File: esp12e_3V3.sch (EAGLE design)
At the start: 26 parts, among them IC1 117\33

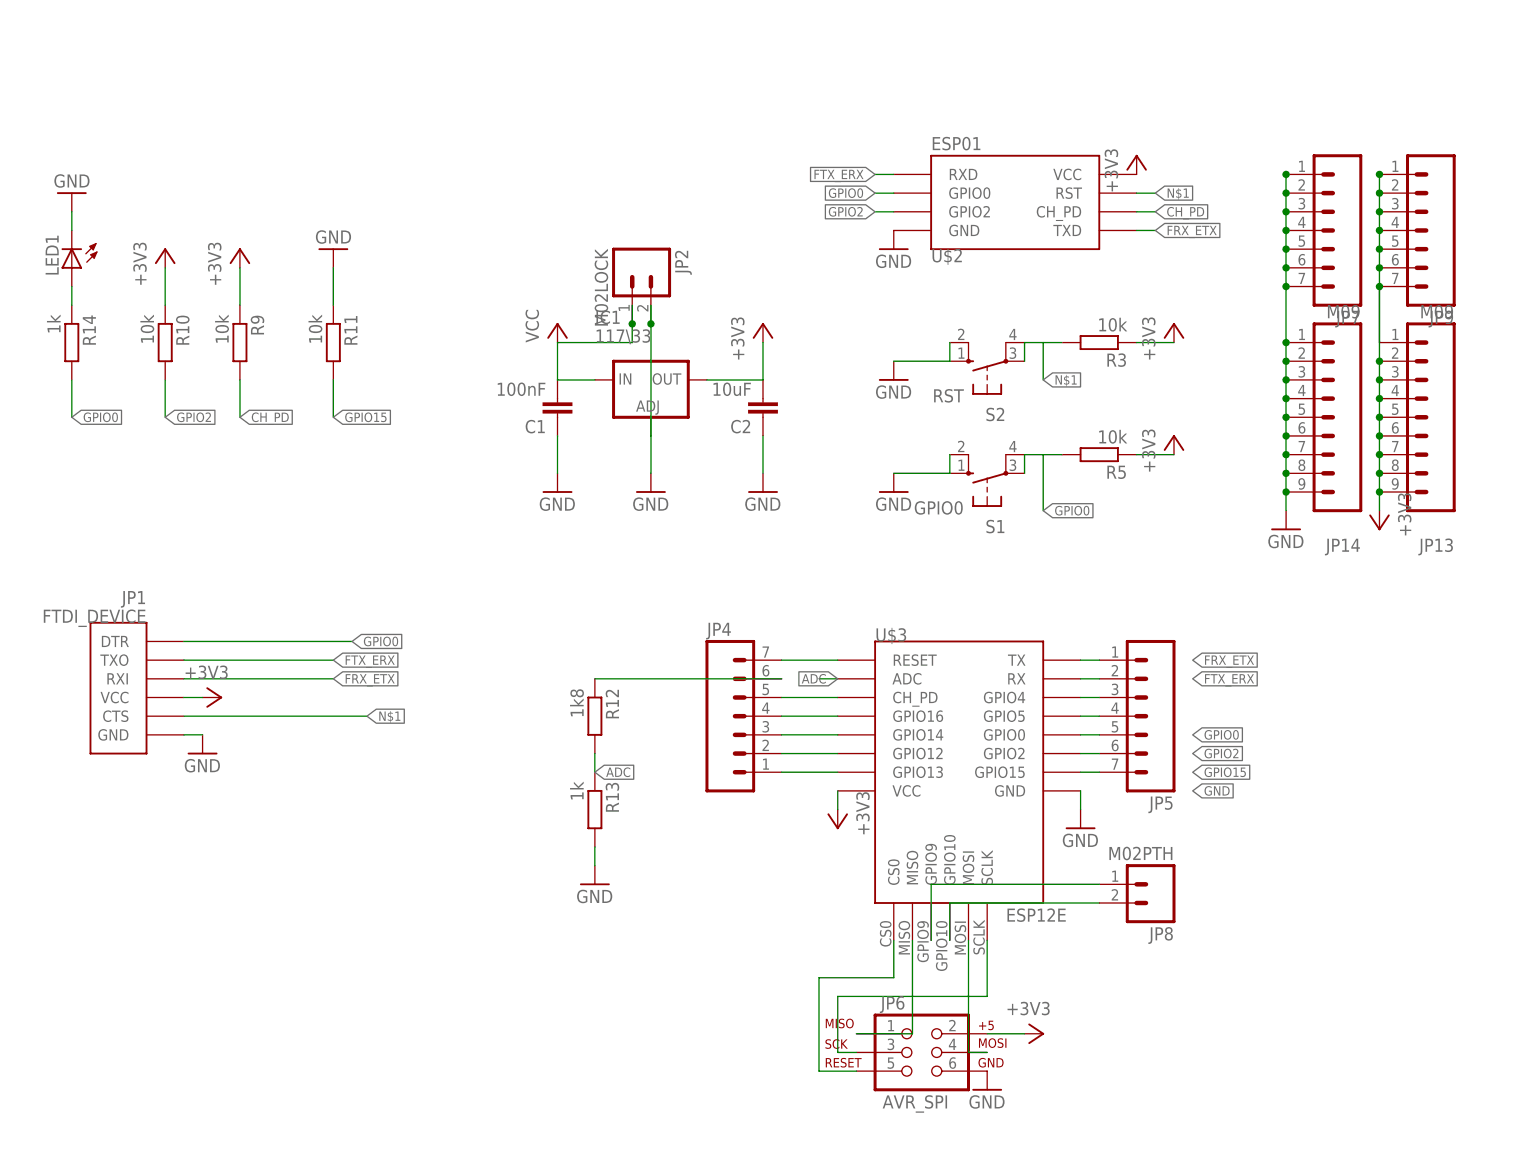
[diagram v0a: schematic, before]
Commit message: esp12e revision
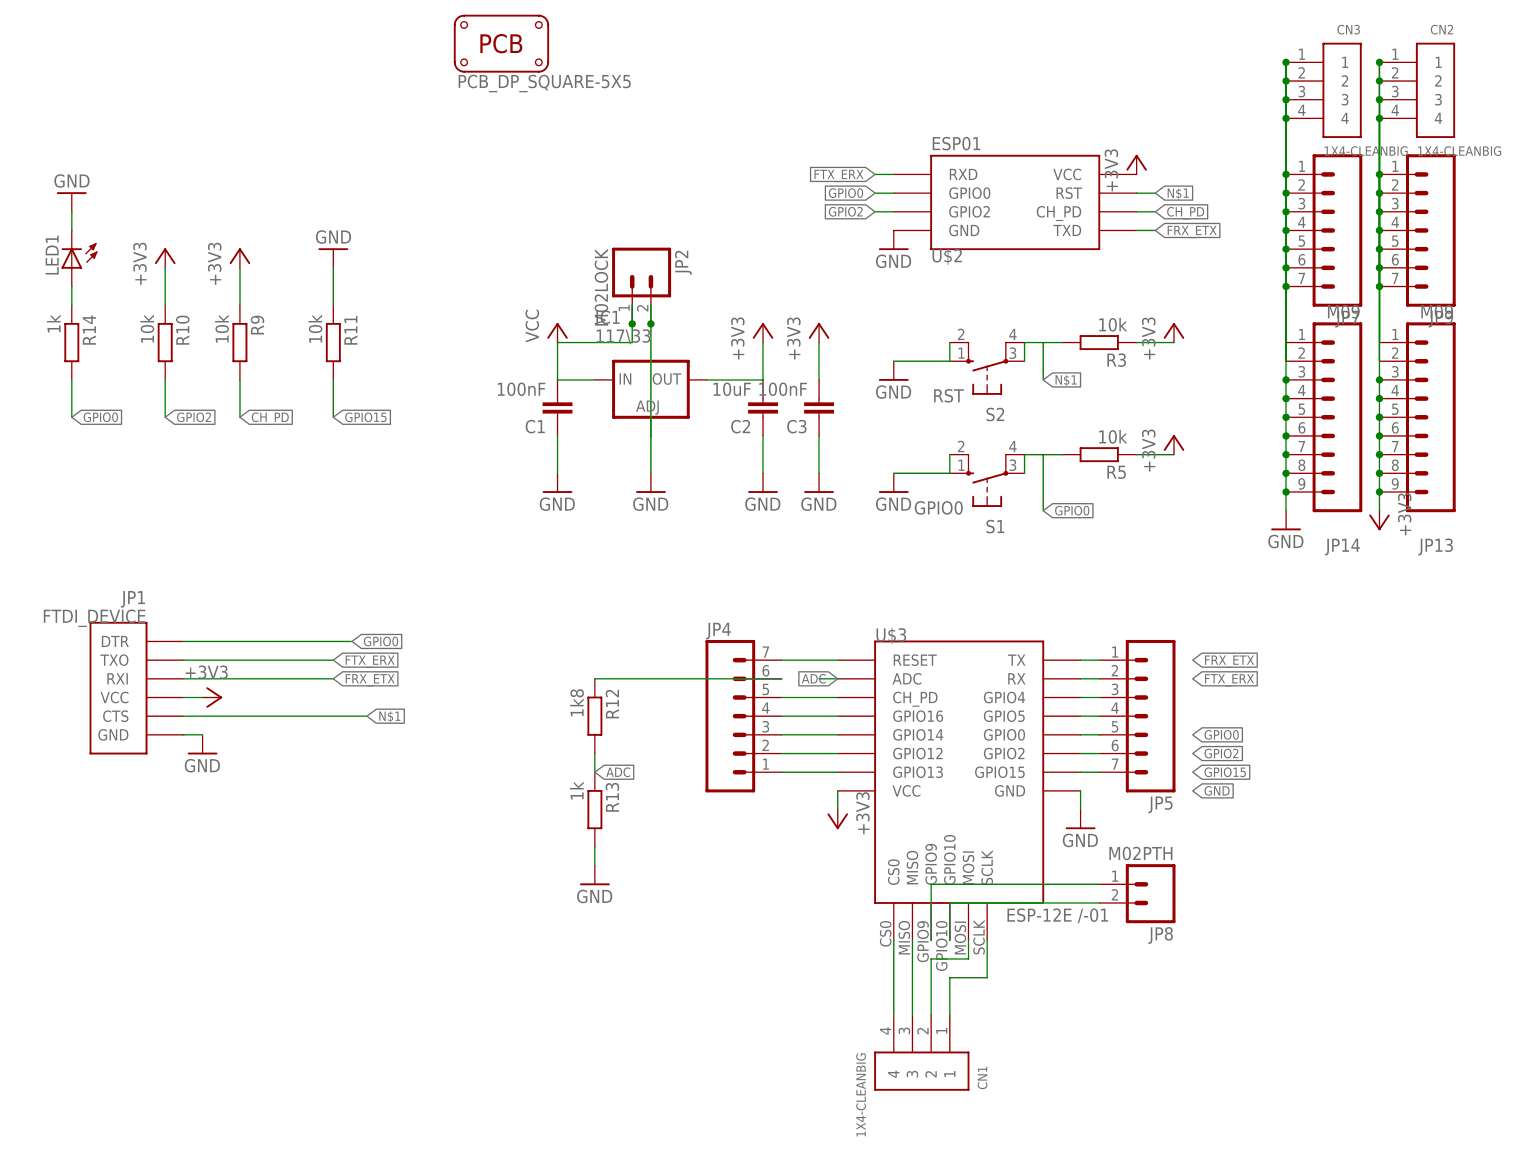
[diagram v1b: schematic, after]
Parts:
- removed JP6: AVR_SPI, SparkFun-Connectors:AVR_SPI_PRG_6NS
- added C3: 100nF, resistor:C-EUC1206
- added CN1, CN2, CN3: 1X4-CLEANBIG, adafruit:1X4-CLEANBIG
- added PCB1: PCB_DP_SQUARE-5X5, dp_pcb:PCB_DP_SQUARE-5X5
- U$3: value ESP12E -> ESP-12E /-01
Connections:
- removed net N$12: JP6.3, U$3.SCLK
- removed net N$13: JP6.5, U$3.CS0
- new net N$2: CN1.4, U$3.CS0
- new net N$6: CN1.3, U$3.MISO
- net +3V3: now also C3.2, CN2.1, CN2.2, CN2.3, CN2.4; no longer JP6.2
- net GND: now also C3.1, CN3.1, CN3.2, CN3.3, CN3.4; no longer JP6.6
- net N$10: now also CN1.2, U$3.MOSI; no longer JP6.1, U$3.MISO
- net N$11: now also CN1.1, U$3.SCLK; no longer JP6.4, U$3.MOSI
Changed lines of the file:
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@@
 <part name="R14" library="resistor" deviceset="R-EU_" device="M1206" value="1k"/>
 <part name="GND15" library="supply1" deviceset="GND" device=""/>
-<part name="U$3" library="esp8266modules" deviceset="ESP12E" device=""/>
+<part name="U$3" library="esp8266modules" deviceset="ESP12E" device="" value="ESP-12E /-01"/>
 <part name="JP4" library="SparkFun-Connectors" deviceset="M07" device=""/>
 <part name="JP5" library="SparkFun-Connectors" deviceset="M07" device=""/>
@@
 <part name="JP13" library="SparkFun-Connectors" deviceset="M09" device=""/>
 <part name="JP14" library="SparkFun-Connectors" deviceset="M09" device=""/>
-<part name="JP6" library="SparkFun-Connectors" deviceset="AVR_SPI_PRG_6" device="NS" value="AVR_SPI"/>
 <part name="JP7" library="SparkFun-Connectors" deviceset="M07" device=""/>
 <part name="JP9" library="SparkFun-Connectors" deviceset="M07" device=""/>
-<part name="GND16" library="supply1" deviceset="GND" device=""/>
-<part name="+3V9" library="supply1" deviceset="+3V3" device=""/>
 <part name="JP2" library="SparkFun-Connectors" deviceset="M02" device="LOCK"/>
 <part name="+3V10" library="supply1" deviceset="+3V3" device=""/>
+<part name="PCB1" library="dp_pcb" deviceset="PCB_DP_SQUARE" device="-5X5"/>
+<part name="+3V13" library="supply1" deviceset="+3V3" device=""/>
+<part name="C3" library="resistor" deviceset="C-EU" device="C1206" value="100nF"/>
+<part name="GND13" library="supply1" deviceset="GND" device=""/>
+<part name="CN1" library="adafruit" deviceset="1X4" device="-CLEANBIG"/>
+<part name="CN2" library="adafruit" deviceset="1X4" device="-CLEANBIG"/>
+<part name="CN3" library="adafruit" deviceset="1X4" device="-CLEANBIG"/>
 </parts>
 <sheets>
@@
 <instance part="JP13" gate="G$1" x="139.7" y="81.28" rot="R180"/>
 <instance part="JP14" gate="G$1" x="127" y="81.28" rot="R180"/>
-<instance part="JP6" gate="G$1" x="66.04" y="-5.08"/>
 <instance part="JP7" gate="G$1" x="121.92" y="109.22" rot="R180"/>
 <instance part="JP9" gate="G$1" x="134.62" y="109.22" rot="R180"/>
-<instance part="GND16" gate="1" x="76.2" y="-10.16"/>
-<instance part="+3V9" gate="G$1" x="83.82" y="-2.54" rot="R270"/>
 <instance part="JP2" gate="G$1" x="27.94" y="101.6" rot="R270"/>
 <instance part="+3V10" gate="G$1" x="-27.94" y="43.18" rot="R270"/>
+<instance part="PCB1" gate="G$1" x="10.16" y="132.08"/>
+<instance part="+3V13" gate="G$1" x="53.34" y="93.98"/>
+<instance part="C3" gate="G$1" x="53.34" y="81.28" rot="R180"/>
+<instance part="GND13" gate="1" x="53.34" y="71.12"/>
+<instance part="CN1" gate="G$1" x="68.58" y="-5.08" rot="R270"/>
+<instance part="CN2" gate="G$1" x="134.62" y="127"/>
+<instance part="CN3" gate="G$1" x="121.92" y="127"/>
 </instances>
 <busses>
@@
 <wire x1="116.84" y1="104.14" x2="116.84" y2="101.6" width="0.1524" layer="91"/>
 <wire x1="116.84" y1="101.6" x2="116.84" y2="99.06" width="0.1524" layer="91"/>
-<wire x1="116.84" y1="99.06" x2="116.84" y2="91.44" width="0.1524" layer="91"/>
-<wire x1="116.84" y1="91.44" x2="116.84" y2="88.9" width="0.1524" layer="91"/>
-<wire x1="116.84" y1="88.9" x2="116.84" y2="86.36" width="0.1524" layer="91"/>
+<wire x1="116.84" y1="99.06" x2="116.84" y2="129.54" width="0.1524" layer="91"/>
+<wire x1="116.84" y1="129.54" x2="116.84" y2="127" width="0.1524" layer="91"/>
+<wire x1="116.84" y1="127" x2="116.84" y2="124.46" width="0.1524" layer="91"/>
+<wire x1="116.84" y1="124.46" x2="116.84" y2="121.92" width="0.1524" layer="91"/>
+<wire x1="116.84" y1="121.92" x2="116.84" y2="86.36" width="0.1524" layer="91"/>
 <wire x1="116.84" y1="86.36" x2="116.84" y2="83.82" width="0.1524" layer="91"/>
 <wire x1="116.84" y1="83.82" x2="116.84" y2="81.28" width="0.1524" layer="91"/>
@@
 <junction x="116.84" y="101.6"/>
 <pinref part="JP14" gate="G$1" pin="1"/>
-<junction x="116.84" y="91.44"/>
+<junction x="116.84" y="124.46"/>
 <pinref part="JP14" gate="G$1" pin="2"/>
-<junction x="116.84" y="88.9"/>
+<junction x="116.84" y="121.92"/>
 <pinref part="JP14" gate="G$1" pin="3"/>
 <junction x="116.84" y="86.36"/>
@@
 <pinref part="JP7" gate="G$1" pin="7"/>
 <junction x="116.84" y="99.06"/>
+<pinref part="CN3" gate="G$1" pin="1"/>
+<junction x="116.84" y="129.54"/>
+<pinref part="CN3" gate="G$1" pin="2"/>
+<junction x="116.84" y="127"/>
+<pinref part="CN3" gate="G$1" pin="3"/>
+<pinref part="CN3" gate="G$1" pin="4"/>
+<wire x1="116.84" y1="121.92" x2="116.84" y2="88.9" width="0.1524" layer="91"/>
+<wire x1="116.84" y1="124.46" x2="116.84" y2="91.44" width="0.1524" layer="91"/>
 </segment>
 <segment>
@@
 </segment>
 <segment>
-<pinref part="JP6" gate="G$1" pin="6"/>
-<pinref part="GND16" gate="1" pin="GND"/>
+<pinref part="GND13" gate="1" pin="GND"/>
+<pinref part="C3" gate="G$1" pin="1"/>
+<wire x1="53.34" y1="73.66" x2="53.34" y2="78.74" width="0.1524" layer="91"/>
 </segment>
 </net>
@@
 <wire x1="129.54" y1="106.68" x2="129.54" y2="104.14" width="0.1524" layer="91"/>
 <wire x1="129.54" y1="104.14" x2="129.54" y2="101.6" width="0.1524" layer="91"/>
-<wire x1="129.54" y1="99.06" x2="129.54" y2="88.9" width="0.1524" layer="91"/>
-<wire x1="129.54" y1="88.9" x2="129.54" y2="86.36" width="0.1524" layer="91"/>
+<wire x1="129.54" y1="124.46" x2="129.54" y2="121.92" width="0.1524" layer="91"/>
+<wire x1="129.54" y1="121.92" x2="129.54" y2="86.36" width="0.1524" layer="91"/>
 <wire x1="129.54" y1="86.36" x2="129.54" y2="83.82" width="0.1524" layer="91"/>
 <wire x1="129.54" y1="83.82" x2="129.54" y2="81.28" width="0.1524" layer="91"/>
@@
 <pinref part="JP13" gate="G$1" pin="1"/>
 <pinref part="JP13" gate="G$1" pin="2"/>
-<junction x="129.54" y="88.9"/>
+<junction x="129.54" y="121.92"/>
 <pinref part="JP13" gate="G$1" pin="3"/>
 <junction x="129.54" y="86.36"/>
@@
 <pinref part="JP9" gate="G$1" pin="6"/>
 <pinref part="JP9" gate="G$1" pin="7"/>
-<wire x1="129.54" y1="99.06" x2="129.54" y2="91.44" width="0.1524" layer="91"/>
+<wire x1="129.54" y1="99.06" x2="129.54" y2="129.54" width="0.1524" layer="91"/>
 <junction x="129.54" y="99.06"/>
+<pinref part="CN2" gate="G$1" pin="1"/>
+<wire x1="129.54" y1="129.54" x2="129.54" y2="127" width="0.1524" layer="91"/>
+<junction x="129.54" y="129.54"/>
+<pinref part="CN2" gate="G$1" pin="2"/>
+<wire x1="129.54" y1="127" x2="129.54" y2="124.46" width="0.1524" layer="91"/>
+<junction x="129.54" y="127"/>
+<pinref part="CN2" gate="G$1" pin="3"/>
+<junction x="129.54" y="124.46"/>
+<pinref part="CN2" gate="G$1" pin="4"/>
+<wire x1="129.54" y1="124.46" x2="129.54" y2="91.44" width="0.1524" layer="91"/>
+<wire x1="129.54" y1="121.92" x2="129.54" y2="88.9" width="0.1524" layer="91"/>
 </segment>
 <segment>
@@
 </segment>
 <segment>
-<pinref part="JP6" gate="G$1" pin="2"/>
-<pinref part="+3V9" gate="G$1" pin="+3V3"/>
-<wire x1="81.28" y1="-2.54" x2="76.2" y2="-2.54" width="0.1524" layer="91"/>
-</segment>
-<segment>
 <pinref part="JP1" gate="G$1" pin="VCC"/>
 <wire x1="-30.48" y1="43.18" x2="-33.02" y2="43.18" width="0.1524" layer="91"/>
 <pinref part="+3V10" gate="G$1" pin="+3V3"/>
+</segment>
+<segment>
+<pinref part="C3" gate="G$1" pin="2"/>
+<pinref part="+3V13" gate="G$1" pin="+3V3"/>
+<wire x1="53.34" y1="86.36" x2="53.34" y2="91.44" width="0.1524" layer="91"/>
 </segment>
 </net>
@@
 </segment>
 </net>
+<net name="N$2" class="0">
+<segment>
+<pinref part="U$3" gate="G$1" pin="CS0"/>
+<pinref part="CN1" gate="G$1" pin="4"/>
+<wire x1="63.5" y1="10.16" x2="63.5" y2="0" width="0.1524" layer="91"/>
+</segment>
+</net>
+<net name="N$6" class="0">
+<segment>
+<pinref part="CN1" gate="G$1" pin="3"/>
+<pinref part="U$3" gate="G$1" pin="MISO"/>
+<wire x1="66.04" y1="0" x2="66.04" y2="10.16" width="0.1524" layer="91"/>
+</segment>
+</net>
 <net name="N$10" class="0">
 <segment>
-<pinref part="U$3" gate="G$1" pin="MISO"/>
-<wire x1="66.04" y1="10.16" x2="66.04" y2="-2.54" width="0.1524" layer="91"/>
-<pinref part="JP6" gate="G$1" pin="1"/>
-<wire x1="66.04" y1="-2.54" x2="58.42" y2="-2.54" width="0.1524" layer="91"/>
+<pinref part="U$3" gate="G$1" pin="MOSI"/>
+<wire x1="73.66" y1="10.16" x2="73.66" y2="7.62" width="0.1524" layer="91"/>
+<pinref part="CN1" gate="G$1" pin="2"/>
+<wire x1="73.66" y1="7.62" x2="68.58" y2="7.62" width="0.1524" layer="91"/>
+<wire x1="68.58" y1="7.62" x2="68.58" y2="0" width="0.1524" layer="91"/>
 </segment>
 </net>
 <net name="N$11" class="0">
 <segment>
-<pinref part="U$3" gate="G$1" pin="MOSI"/>
-<wire x1="73.66" y1="10.16" x2="73.66" y2="-5.08" width="0.1524" layer="91"/>
-<pinref part="JP6" gate="G$1" pin="4"/>
-<wire x1="73.66" y1="-5.08" x2="76.2" y2="-5.08" width="0.1524" layer="91"/>
-</segment>
-</net>
-<net name="N$12" class="0">
-<segment>
-<pinref part="JP6" gate="G$1" pin="3"/>
-<wire x1="58.42" y1="-5.08" x2="55.88" y2="-5.08" width="0.1524" layer="91"/>
-<wire x1="55.88" y1="-5.08" x2="55.88" y2="2.54" width="0.1524" layer="91"/>
 <pinref part="U$3" gate="G$1" pin="SCLK"/>
-<wire x1="55.88" y1="2.54" x2="76.2" y2="2.54" width="0.1524" layer="91"/>
-<wire x1="76.2" y1="2.54" x2="76.2" y2="10.16" width="0.1524" layer="91"/>
-</segment>
-</net>
-<net name="N$13" class="0">
-<segment>
-<pinref part="U$3" gate="G$1" pin="CS0"/>
-<wire x1="63.5" y1="10.16" x2="63.5" y2="5.08" width="0.1524" layer="91"/>
-<wire x1="63.5" y1="5.08" x2="53.34" y2="5.08" width="0.1524" layer="91"/>
-<wire x1="53.34" y1="5.08" x2="53.34" y2="-7.62" width="0.1524" layer="91"/>
-<pinref part="JP6" gate="G$1" pin="5"/>
-<wire x1="53.34" y1="-7.62" x2="58.42" y2="-7.62" width="0.1524" layer="91"/>
-</segment>
-</net>
+<wire x1="76.2" y1="10.16" x2="76.2" y2="5.08" width="0.1524" layer="91"/>
+<pinref part="CN1" gate="G$1" pin="1"/>
+<wire x1="76.2" y1="5.08" x2="71.12" y2="5.08" width="0.1524" layer="91"/>
+<wire x1="71.12" y1="5.08" x2="71.12" y2="0" width="0.1524" layer="91"/>
+</segment>
+</net>
